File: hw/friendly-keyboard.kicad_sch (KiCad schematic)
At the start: 1 part

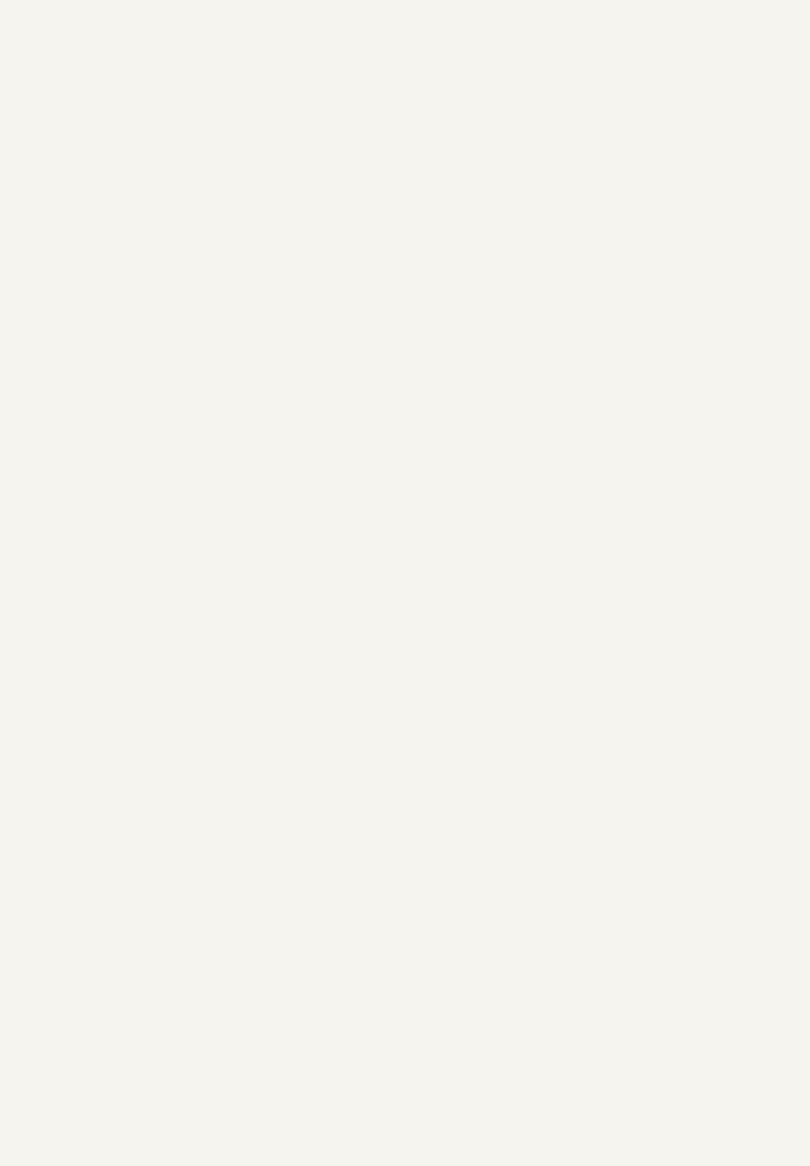
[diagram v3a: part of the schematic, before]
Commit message: Cypress USB interface symbol & Layout needs fixing
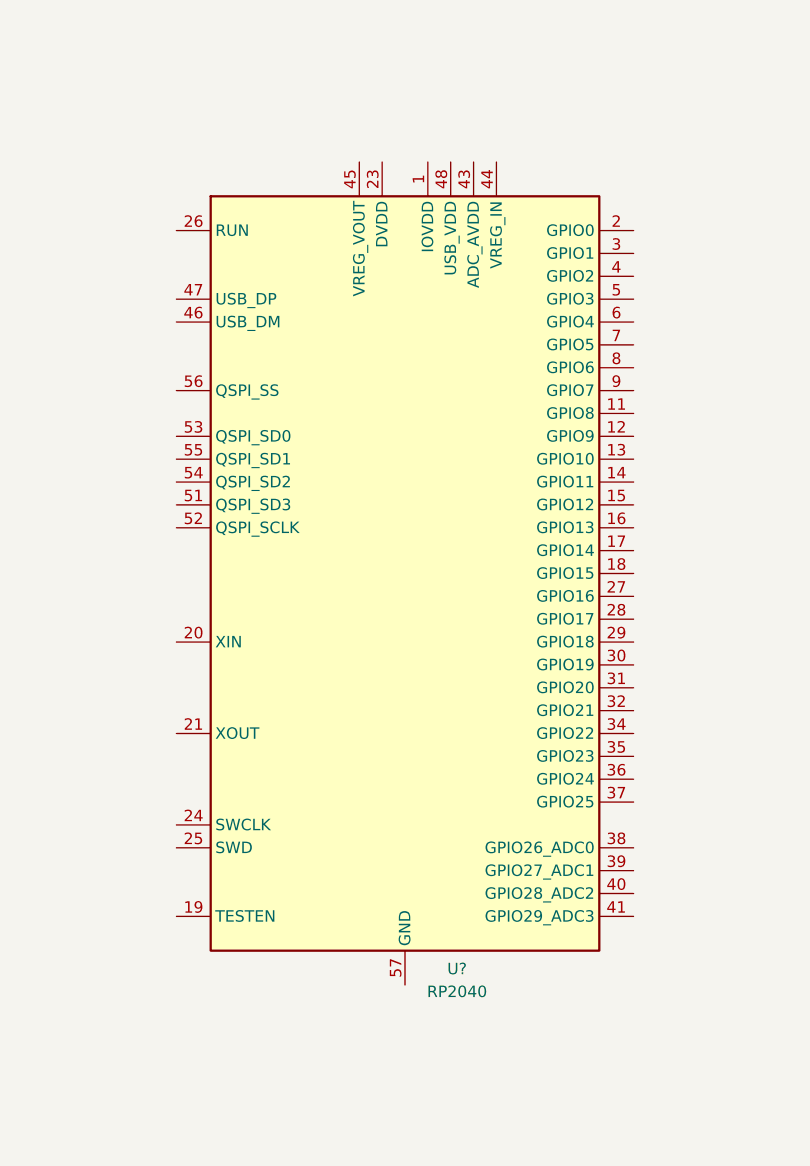
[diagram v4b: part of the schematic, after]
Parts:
- added U?: RP2040, Package_DFN_QFN:QFN-56-1EP_7x7mm_P0.4mm_EP3.2x3.2mm, symbol MCU_RaspberryPi:RP2040
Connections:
- new net: U?.1 (IOVDD), U?.10 (IOVDD), U?.22 (IOVDD), U?.33 (IOVDD), U?.42 (IOVDD), U?.49 (IOVDD)
- new net: U?.23 (DVDD), U?.50 (DVDD)
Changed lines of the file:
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@@
+    (pin "9")
+  )
+  (symbol (lib_id "MCU_RaspberryPi:RP2040") (at 293.37 106.68 0) (unit 1)
+    (in_bom yes) (on_board yes) (fields_autoplaced)
+    (property "Reference" "U?" (id 0) (at 299.1578 150.6204 0))
+    (property "Value" "RP2040" (id 1) (at 299.1578 153.1573 0))
+    (property "Footprint" "Package_DFN_QFN:QFN-56-1EP_7x7mm_P0.4mm_EP3.2x3.2mm" (id 2) (at 293.37 106.68 0)
+      (effects (font (size 1.27 1.27)) hide)
+    )
+    (property "Datasheet" "https://datasheets.raspberrypi.com/rp2040/rp2040-datasheet.pdf" (id 3) (at 293.37 106.68 0)
+      (effects (font (size 1.27 1.27)) hide)
+    )
+    (pin "1")
+    (pin "10")
+    (pin "11")
+    (pin "12")
+    (pin "13")
+    (pin "14")
+    (pin "15")
+    (pin "16")
+    (pin "17")
+    (pin "18")
+    (pin "19")
+    (pin "2")
+    (pin "20")
+    (pin "21")
+    (pin "22")
+    (pin "23")
+    (pin "24")
+    (pin "25")
+    (pin "26")
+    (pin "27")
+    (pin "28")
+    (pin "29")
+    (pin "3")
+    (pin "30")
+    (pin "31")
+    (pin "32")
+    (pin "33")
+    (pin "34")
+    (pin "35")
+    (pin "36")
+    (pin "37")
+    (pin "38")
+    (pin "39")
+    (pin "4")
+    (pin "40")
+    (pin "41")
+    (pin "42")
+    (pin "43")
+    (pin "44")
+    (pin "45")
+    (pin "46")
+    (pin "47")
+    (pin "48")
+    (pin "49")
+    (pin "5")
+    (pin "50")
+    (pin "51")
+    (pin "52")
+    (pin "53")
+    (pin "54")
+    (pin "55")
+    (pin "56")
+    (pin "57")
+    (pin "6")
+    (pin "7")
+    (pin "8")
     (pin "9")
   )
@@
       (reference "#PWR?") (unit 1) (value "GND") (footprint "")
     )
+    (path "/8573b0fd-89cc-41d3-aea1-2aec3a4f41a4/2105b185-5d37-47e7-8fe3-6d3ee2ed4972"
+      (reference "#PWR?") (unit 1) (value "VBUS") (footprint "")
+    )
     (path "/a9b596e6-e9c2-406e-b1ff-0f528e1fa26a/2638a179-bec3-4642-ae1a-3fb8edb7bedf"
       (reference "#PWR?") (unit 1) (value "GND") (footprint "")
@@
       (reference "U?") (unit 1) (value "W25Q128JVSS") (footprint "Package_SO:SOIC-8_5.23x5.23mm_P1.27mm")
     )
+    (path "/a62adf64-0bba-43c6-8dc5-f8e70a731994"
+      (reference "U?") (unit 1) (value "RP2040") (footprint "Package_DFN_QFN:QFN-56-1EP_7x7mm_P0.4mm_EP3.2x3.2mm")
+    )
     (path "/a9b596e6-e9c2-406e-b1ff-0f528e1fa26a/c4fdc52d-7d0b-4e32-b455-42feeaa12419"
